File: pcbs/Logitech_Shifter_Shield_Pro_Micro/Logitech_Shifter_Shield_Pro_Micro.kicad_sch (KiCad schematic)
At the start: 12 parts, among them J1 DB9_Male_MountingHoles, J2 AVR-ISP-6, U1 SparkFun_ProMicro

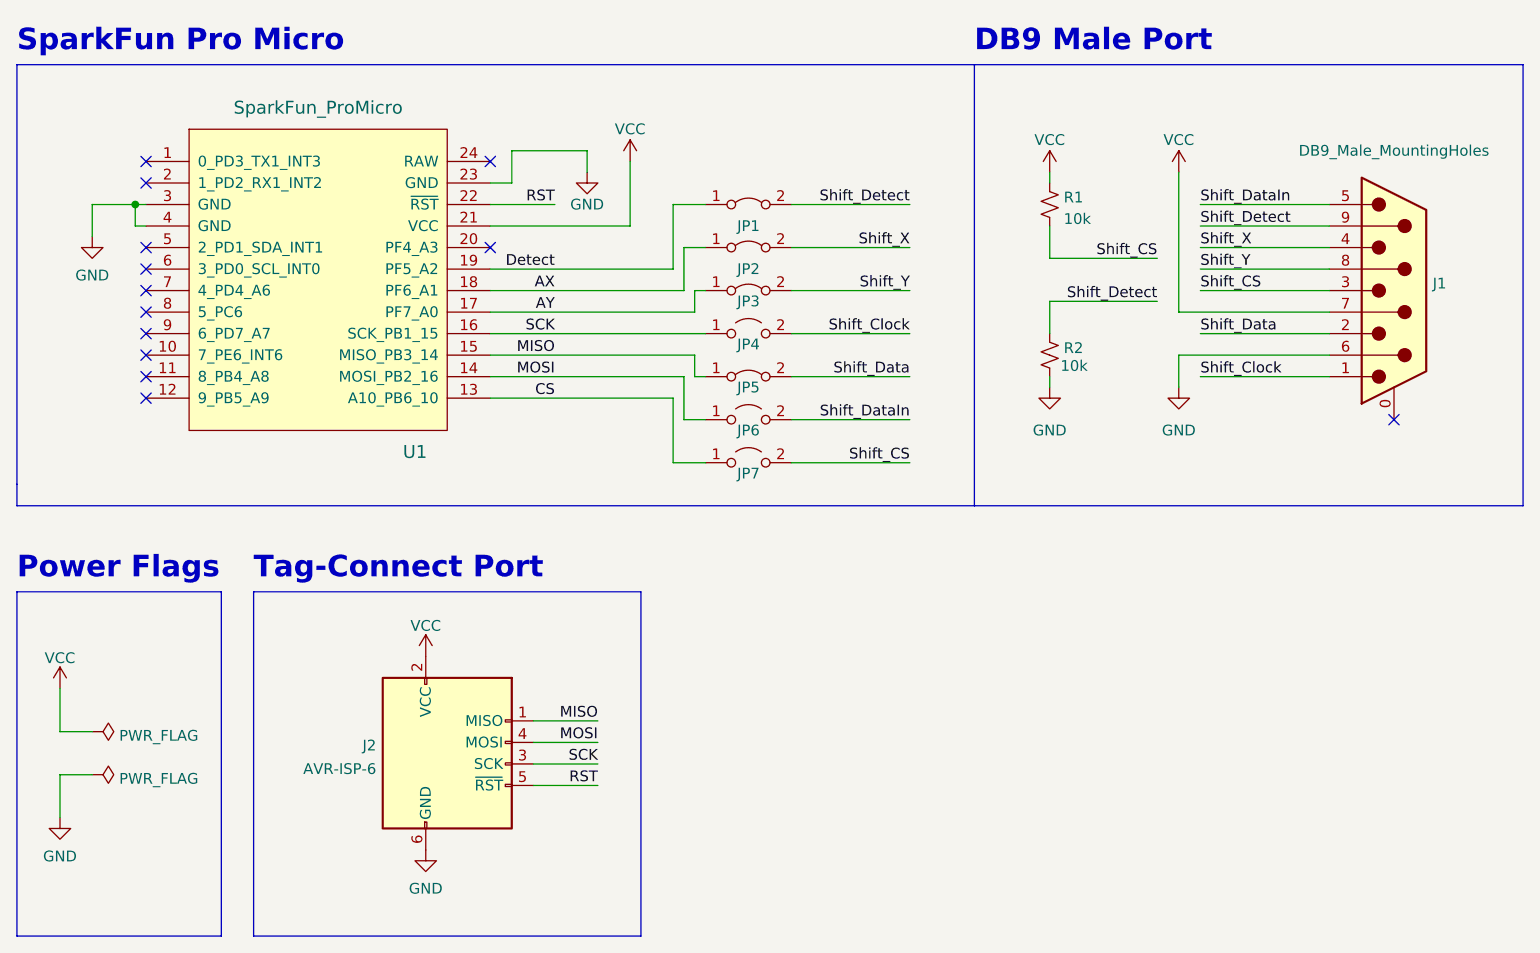
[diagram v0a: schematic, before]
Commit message: Update PCBs to KiCad8 format (8.0.8)
No intended functional changes. Open -> Save -> Close.
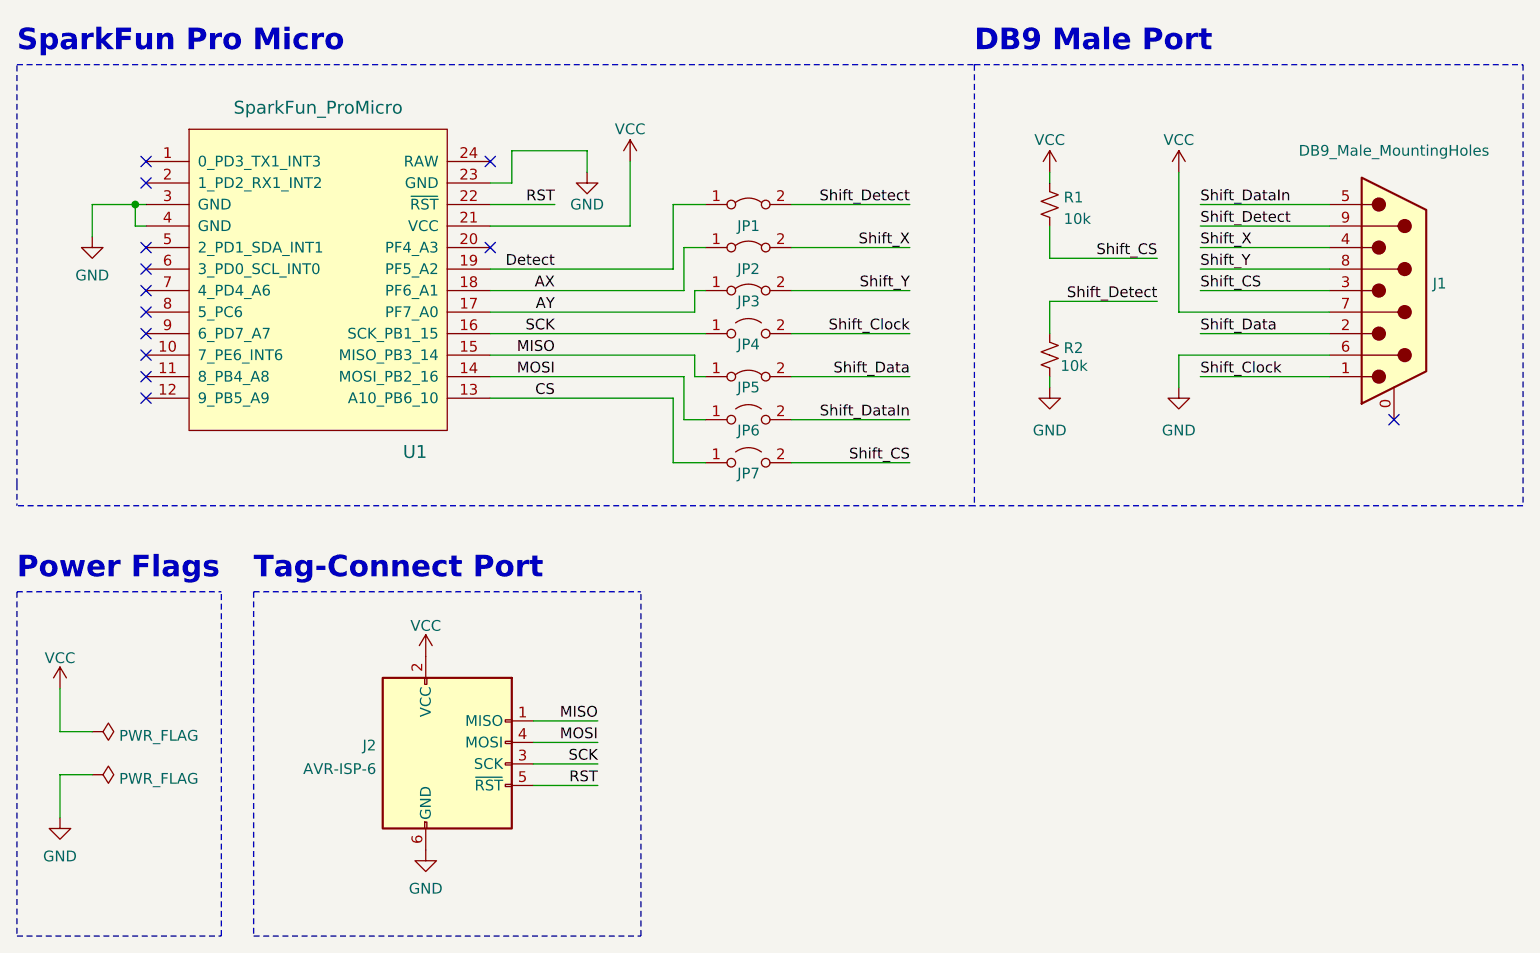
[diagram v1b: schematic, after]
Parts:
- JP1, JP2, JP3, JP5: footprint (none) -> Sim_Racing_Shields:SolderJumper-2_P1.3mm_Bridged_RoundedPad1.0x1.5mm_Unmasked
- U1: footprint (none) -> Sim_Racing_Shields:Sparkfun_ProMicro

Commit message: Relink DE-9 connector symbols (KiCad8)
These symbol names' changed in the included KiCad library.
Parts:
- J1: value DB9_Male_MountingHoles -> DE9_Plug_MountingHoles; symbol Connector:DB9_Male_MountingHoles -> Connector:DE9_Plug_MountingHoles
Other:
- note added: "DE9 Male Port"
- note removed: "DB9 Male Port"
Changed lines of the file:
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@@
 		)
 	)
-	(text "DB9 Male Port"
+	(text "DE9 Male Port"
 		(exclude_from_sim no)
 		(at 171.45 48.26 0)
@@
 	)
 	(symbol
-		(lib_id "Connector:DB9_Male_MountingHoles")
+		(lib_id "Connector:DE9_Plug_MountingHoles")
 		(at 220.98 76.2 0)
 		(unit 1)
@@
 			)
 		)
-		(property "Value" "DB9_Male_MountingHoles"
+		(property "Value" "DE9_Plug_MountingHoles"
 			(at 220.98 59.69 0)
 			(effects
@@
 			)
 		)
-		(property "Datasheet" " ~"
+		(property "Datasheet" "~"
 			(at 220.98 76.2 0)
 			(effects
@@
 			)
 		)
-		(property "Description" ""
+		(property "Description" "9-pin male plug pin D-SUB connector, Mounting Hole"
 			(at 220.98 76.2 0)
 			(effects
